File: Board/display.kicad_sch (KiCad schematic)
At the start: 6 parts, among them U3 Display_ILI9341

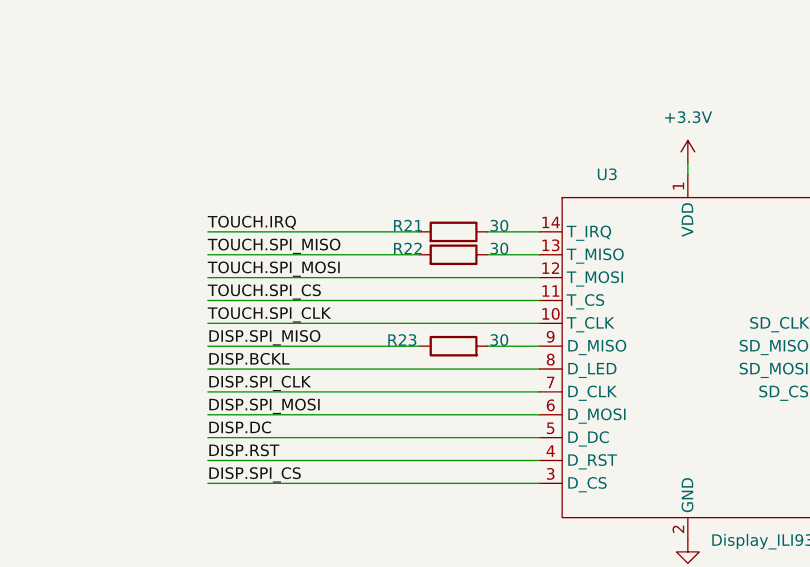
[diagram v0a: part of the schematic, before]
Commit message: Add I2C pin header
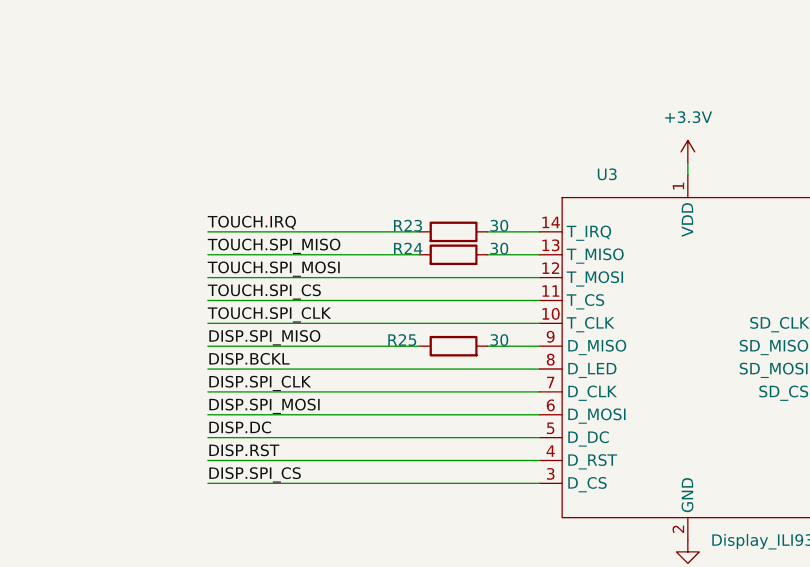
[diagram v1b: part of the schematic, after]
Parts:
- renumbered R21 to R23, R22 to R24, R23 to R25
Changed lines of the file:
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@@
   (symbol (lib_id "power:+3.3V") (at 99.06 30.48 0) (unit 1)
     (in_bom yes) (on_board yes) (fields_autoplaced)
-    (property "Reference" "#PWR028" (id 0) (at 99.06 34.29 0)
+    (property "Reference" "#PWR031" (id 0) (at 99.06 34.29 0)
       (effects (font (size 1.27 1.27)) hide)
     )
@@
   (symbol (lib_id "power:+3.3V") (at 138.43 64.77 0) (unit 1)
     (in_bom yes) (on_board yes) (fields_autoplaced)
-    (property "Reference" "#PWR030" (id 0) (at 138.43 68.58 0)
+    (property "Reference" "#PWR033" (id 0) (at 138.43 68.58 0)
       (effects (font (size 1.27 1.27)) hide)
     )
@@
   (symbol (lib_id "Device:R") (at 112.395 74.93 270) (mirror x) (unit 1)
     (in_bom yes) (on_board yes)
-    (property "Reference" "R22" (id 0) (at 107.315 74.295 90))
+    (property "Reference" "R24" (id 0) (at 107.315 74.295 90))
     (property "Value" "30" (id 1) (at 117.475 74.295 90))
     (property "Footprint" "Resistor_SMD:R_0603_1608Metric_Pad0.98x0.95mm_HandSolder" (id 2) (at 112.395 76.708 90)
@@
   (symbol (lib_id "Device:R") (at 112.395 85.09 90) (unit 1)
     (in_bom yes) (on_board yes)
-    (property "Reference" "R23" (id 0) (at 106.68 84.455 90))
+    (property "Reference" "R25" (id 0) (at 106.68 84.455 90))
     (property "Value" "30" (id 1) (at 117.475 84.455 90))
     (property "Footprint" "Resistor_SMD:R_0603_1608Metric_Pad0.98x0.95mm_HandSolder" (id 2) (at 112.395 86.868 90)
@@
   (symbol (lib_id "power:GND") (at 138.43 106.68 0) (unit 1)
     (in_bom yes) (on_board yes) (fields_autoplaced)
-    (property "Reference" "#PWR031" (id 0) (at 138.43 113.03 0)
+    (property "Reference" "#PWR034" (id 0) (at 138.43 113.03 0)
       (effects (font (size 1.27 1.27)) hide)
     )
@@
   (symbol (lib_id "Device:R") (at 112.395 72.39 270) (mirror x) (unit 1)
     (in_bom yes) (on_board yes)
-    (property "Reference" "R21" (id 0) (at 107.315 71.755 90))
+    (property "Reference" "R23" (id 0) (at 107.315 71.755 90))
     (property "Value" "30" (id 1) (at 117.475 71.755 90))
     (property "Footprint" "Resistor_SMD:R_0603_1608Metric_Pad0.98x0.95mm_HandSolder" (id 2) (at 112.395 74.168 90)
@@
   (symbol (lib_id "power:GND") (at 99.06 38.1 0) (unit 1)
     (in_bom yes) (on_board yes) (fields_autoplaced)
-    (property "Reference" "#PWR029" (id 0) (at 99.06 44.45 0)
+    (property "Reference" "#PWR032" (id 0) (at 99.06 44.45 0)
       (effects (font (size 1.27 1.27)) hide)
     )

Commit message: Add fiducials
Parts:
- renumbered R23 to R25, R24 to R26, R25 to R27
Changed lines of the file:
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@@
   (title_block
     (title "Display")
-    (date "2022/01/17")
+    (date "2022/01/18")
     (rev "v0.1")
     (company "Bzgec")
@@
   (symbol (lib_id "Device:R") (at 112.395 74.93 270) (mirror x) (unit 1)
     (in_bom yes) (on_board yes)
-    (property "Reference" "R24" (id 0) (at 107.315 74.295 90))
+    (property "Reference" "R26" (id 0) (at 107.315 74.295 90))
     (property "Value" "30" (id 1) (at 117.475 74.295 90))
     (property "Footprint" "Resistor_SMD:R_0603_1608Metric_Pad0.98x0.95mm_HandSolder" (id 2) (at 112.395 76.708 90)
@@
   (symbol (lib_id "Device:R") (at 112.395 85.09 90) (unit 1)
     (in_bom yes) (on_board yes)
-    (property "Reference" "R25" (id 0) (at 106.68 84.455 90))
+    (property "Reference" "R27" (id 0) (at 106.68 84.455 90))
     (property "Value" "30" (id 1) (at 117.475 84.455 90))
     (property "Footprint" "Resistor_SMD:R_0603_1608Metric_Pad0.98x0.95mm_HandSolder" (id 2) (at 112.395 86.868 90)
@@
   (symbol (lib_id "Device:R") (at 112.395 72.39 270) (mirror x) (unit 1)
     (in_bom yes) (on_board yes)
-    (property "Reference" "R23" (id 0) (at 107.315 71.755 90))
+    (property "Reference" "R25" (id 0) (at 107.315 71.755 90))
     (property "Value" "30" (id 1) (at 117.475 71.755 90))
     (property "Footprint" "Resistor_SMD:R_0603_1608Metric_Pad0.98x0.95mm_HandSolder" (id 2) (at 112.395 74.168 90)
